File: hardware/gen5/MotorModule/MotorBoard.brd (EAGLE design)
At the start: 60.9 x 49.7 mm, 46 parts, among them IC2 3.3V REG, J1 M20X2SHROUDED

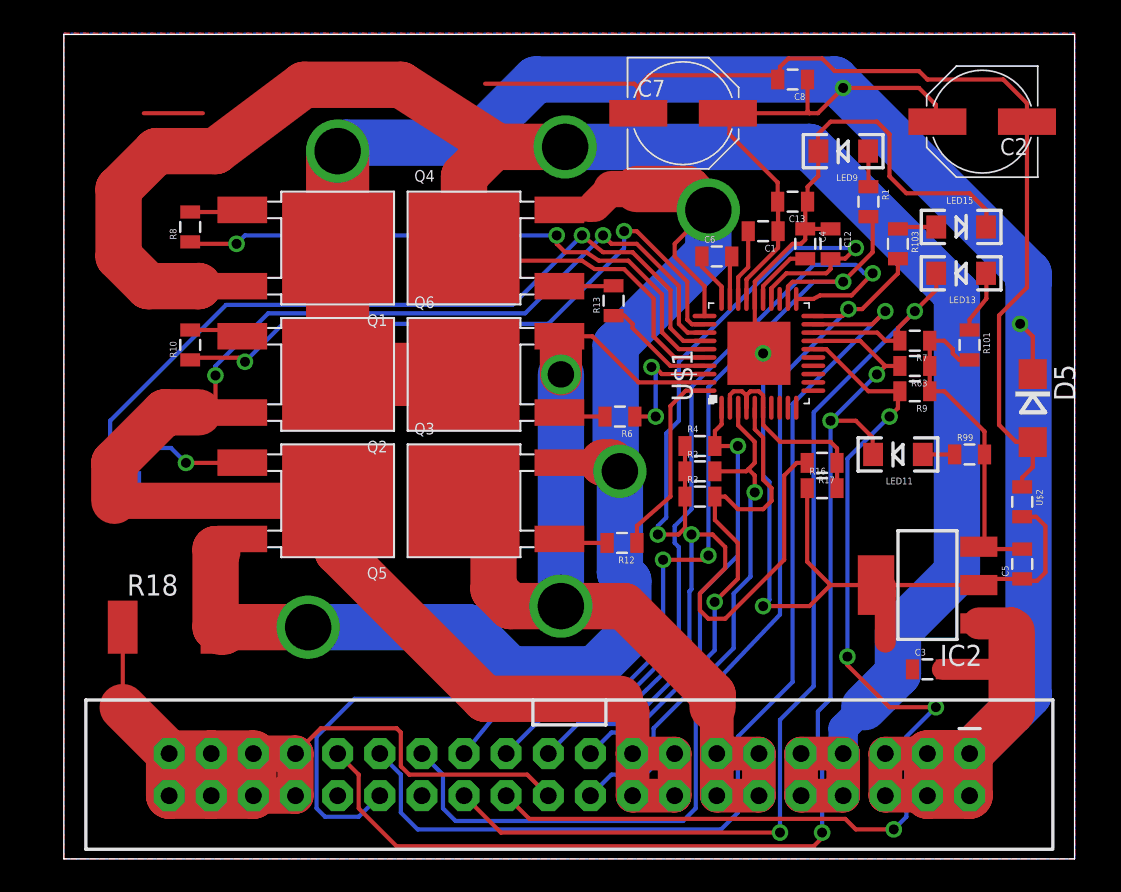
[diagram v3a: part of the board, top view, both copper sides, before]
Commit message: updated motor board
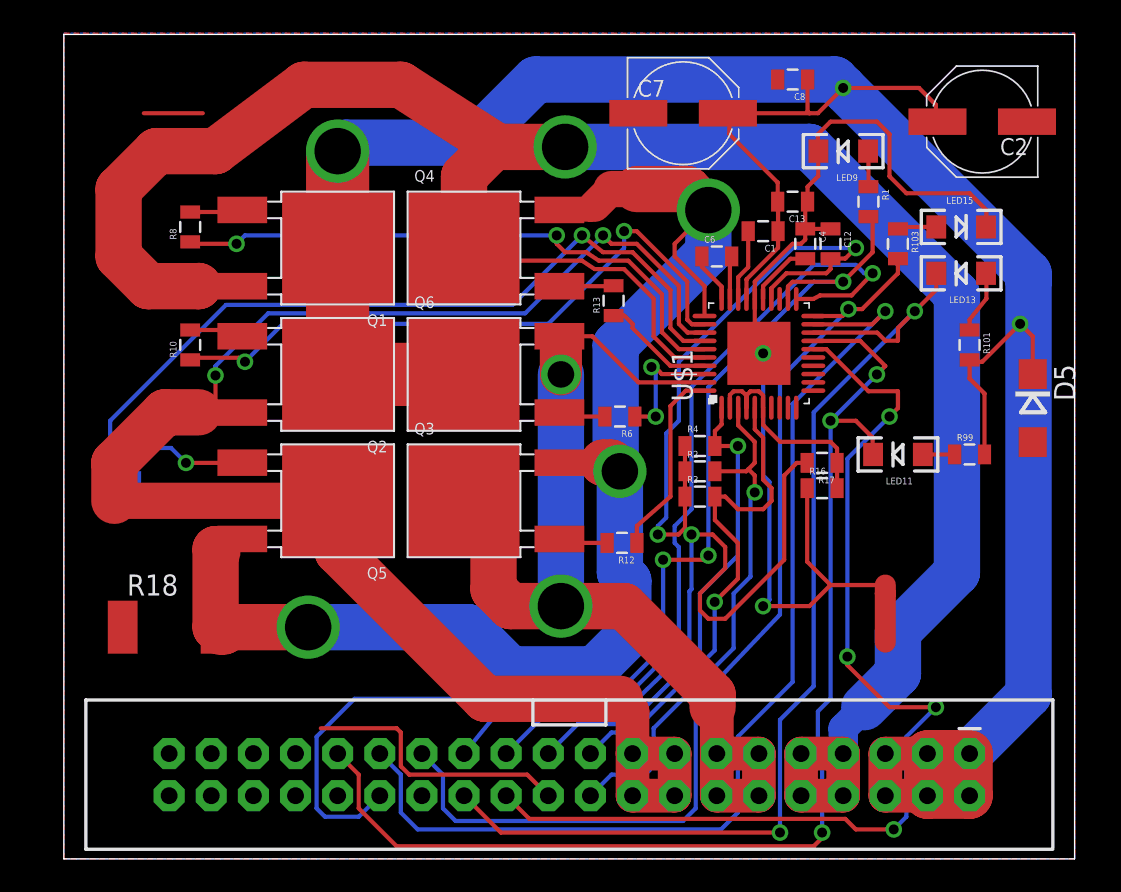
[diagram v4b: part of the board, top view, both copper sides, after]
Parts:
- removed C3, C5: .1uF, SparkFun-Capacitors:0805
- removed IC2: 3.3V REG, linear-technology:SOT223
- removed R63, R7, R9: 1k, SparkFun-Resistors:0805
- removed U$2: INDUCTOR, gen3:0805
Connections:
- removed net 12VGND: C2.-, C3.1, C7.-, C8.2, D5.A, J1.22, J1.33, J1.34, J1.35, J1.36, J1.37, J1.38, J1.39, J1.40, R18.1, U$2.1
- removed net 3.3V: C5.2, IC2.3, R101.2, R63.1, R7.1, R9.1, R99.2
- net 12V: now also R101.2, R99.2; no longer C3.2, IC2.1
- net FAULTN: no longer R63.2
- net GND: now also C2.-, C7.-, C8.2, D5.A, J1.22, J1.33, J1.34, J1.35, J1.36, J1.37, J1.38, J1.39, J1.40, R18.1; no longer C5.1, IC2.2, IC2.4, U$2.2
- net HALLOUT: no longer R9.2
- net LOCKN: no longer R7.2
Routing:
- net 12VGND: track 125.0 -> 0.00 mm
- net 3.3V: track 20.1 -> 0.00 mm
- net GND: track 80.8 -> 86.4 mm
- net 12V: track 171.3 -> 166.4 mm
- net FAULTN: track 73.0 -> 72.1 mm
- added copper zone on layer 1, net GND
- added copper zone on layer 16, net GND
- removed copper zone on layer 1, net 12VGND
- removed copper zone on layer 16, net 12VGND

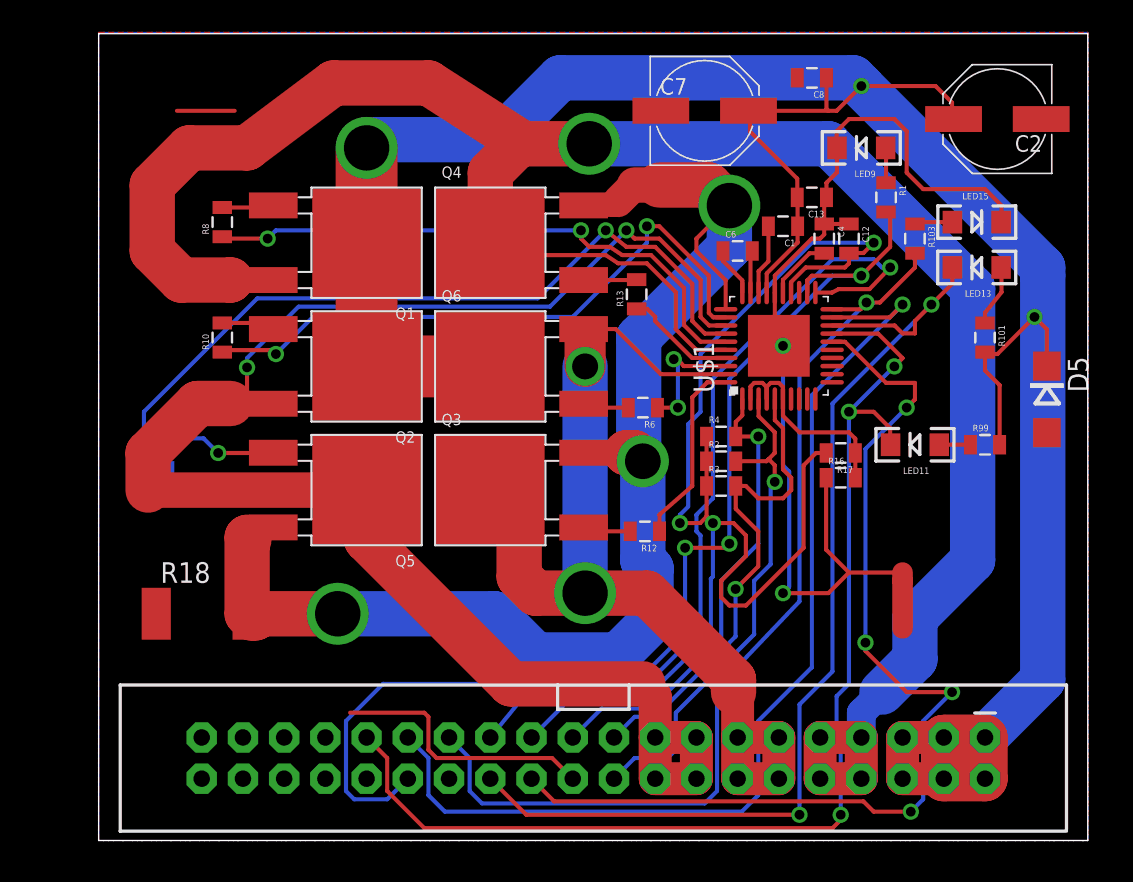
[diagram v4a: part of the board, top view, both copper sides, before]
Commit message: added pullups to the motorboard, and did DRC checking
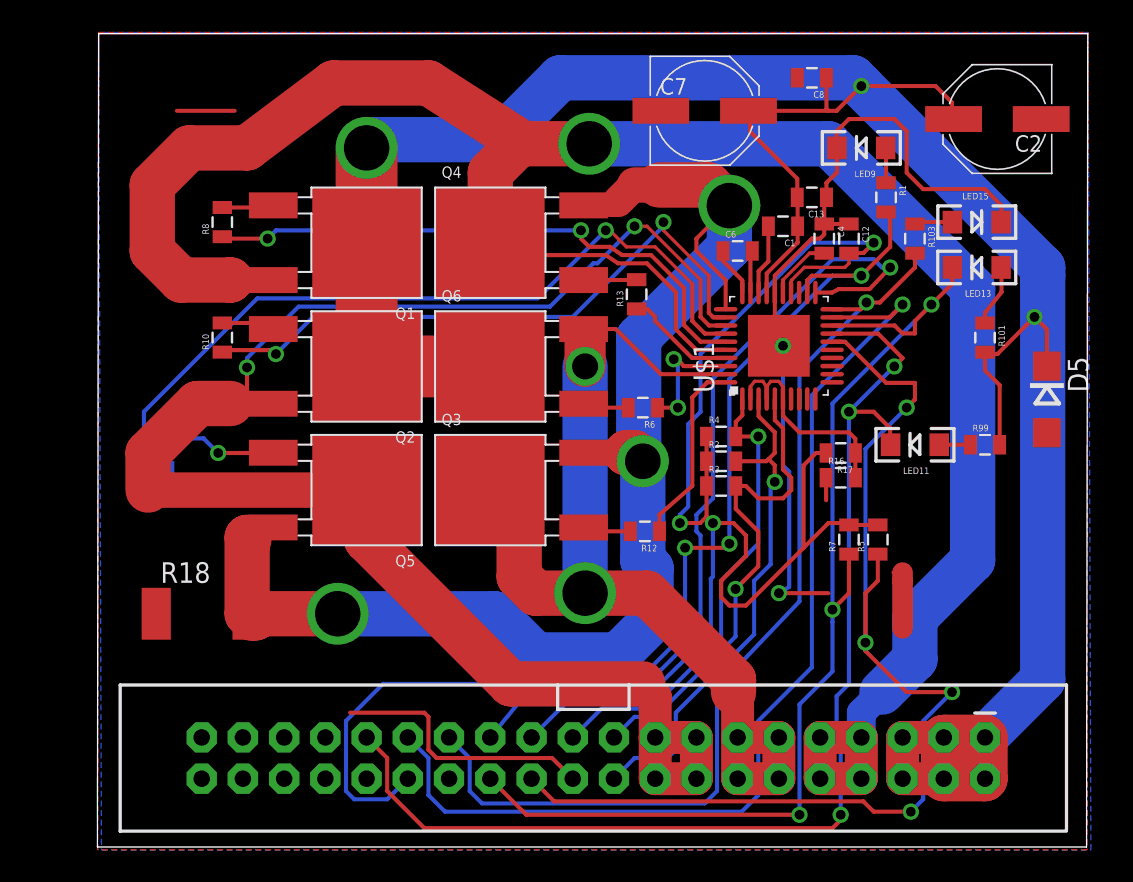
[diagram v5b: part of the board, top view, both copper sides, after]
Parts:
- added R5, R7: 10k, SparkFun-Resistors:0805
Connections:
- net 5V: now also R5.2, R7.2
- net HALLOUT: now also R5.1
- net LOCKN: now also R7.1
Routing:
- net GND: track 86.4 -> 77.3 mm
- net HALLOUT: track 62.9 -> 68.7 mm
- net 5V: track 79.7 -> 85.0 mm
- net LOCKN: track 65.1 -> 68.9 mm, vias 2 -> 3
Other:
- board size 60.9 x 49.7 mm -> 61 x 50.1 mm

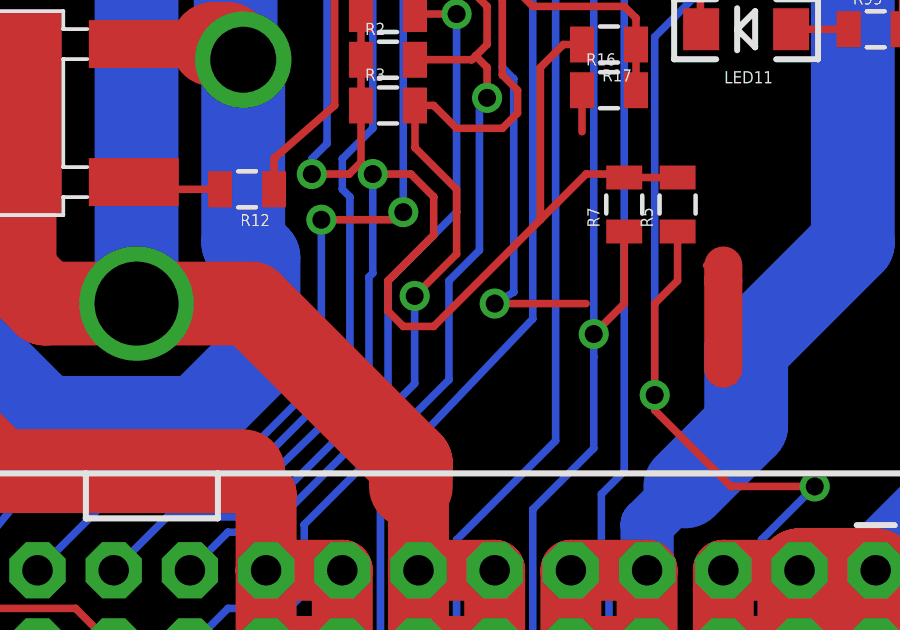
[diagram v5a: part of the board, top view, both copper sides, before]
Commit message: added motorboard gerbers, but noticed some potential issues with grounding afterwards. Checking into it now. It appears that the commsboard is ready to go, however
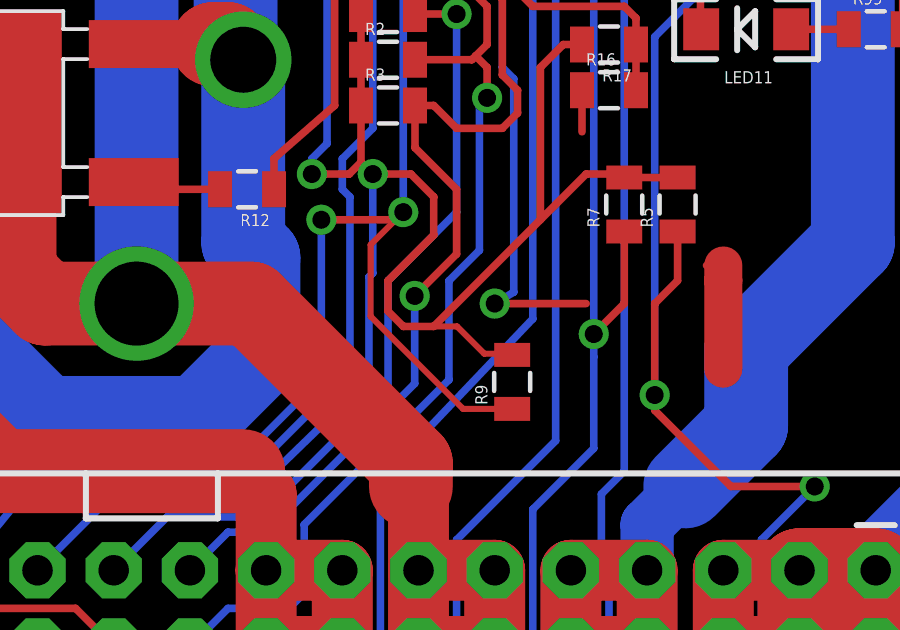
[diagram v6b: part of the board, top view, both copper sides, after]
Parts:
- added R9: 0, SparkFun-Resistors:0805
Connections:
- net 5V: now also R9.2
- net ENABLE: now also R9.1
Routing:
- net ENABLE: track 70.0 -> 79.9 mm
- net 5V: track 85.0 -> 88.1 mm
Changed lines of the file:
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@@
 <wire x1="60.94" y1="49.708" x2="0" y2="49.708" width="0" layer="20"/>
 <wire x1="0" y1="49.708" x2="-0.075796875" y2="-0.398103125" width="0" layer="20"/>
+<dimension x1="60.94" y1="49.708" x2="0" y2="49.708" x3="30.47" y3="53.998428125" textsize="1.778" layer="20" unit="inch"/>
+<dimension x1="61.13459375" y1="-0.5823" x2="60.96" y2="49.784" x3="66.12306875" y3="24.61844375" textsize="1.778" layer="20" unit="inch"/>
 </plain>
 <attributes>
@@
 <element name="R5" library="SparkFun-Resistors" package="0805" value="10k" x="48.006" y="18.542" rot="R90"/>
 <element name="R7" library="SparkFun-Resistors" package="0805" value="10k" x="46.228" y="18.542" rot="R90"/>
+<element name="R9" library="SparkFun-Resistors" package="0805" value="0" x="42.49169375" y="12.629140625" rot="R90"/>
 </elements>
 <signals>
@@
 <wire x1="48.768" y1="36.576" x2="48.768" y2="38.47" width="0.254" layer="1"/>
 <wire x1="48.768" y1="38.47" x2="48.514" y2="38.724" width="0.254" layer="1"/>
+<contactref element="R9" pad="1"/>
+<wire x1="42.49169375" y1="11.729140625" x2="40.85819375" y2="11.729140625" width="0.2032" layer="1"/>
+<wire x1="40.85819375" y1="11.729140625" x2="37.77360625" y2="14.813728125" width="0.2032" layer="1"/>
+<wire x1="37.77360625" y1="14.813728125" x2="37.77360625" y2="17.19960625" width="0.2032" layer="1"/>
+<wire x1="37.77360625" y1="17.19960625" x2="38.862" y2="18.288" width="0.2032" layer="1"/>
 </signal>
 <signal name="DIR">
@@
 <wire x1="42.66030625" y1="34.40530625" x2="42.7151875" y2="34.55069375" width="0.2032" layer="1"/>
 <wire x1="42.7151875" y1="34.55069375" x2="43.480784375" y2="35.316290625" width="0.2032" layer="1"/>
+<contactref element="R9" pad="2"/>
+<wire x1="39.878" y1="14.478" x2="40.654153125" y2="14.478" width="0.2032" layer="1"/>
+<wire x1="40.654153125" y1="14.478" x2="41.562625" y2="13.569528125" width="0.2032" layer="1"/>
+<wire x1="41.562625" y1="13.569528125" x2="42.45130625" y2="13.569528125" width="0.2032" layer="1"/>
+<wire x1="42.45130625" y1="13.569528125" x2="42.49169375" y2="13.529140625" width="0.2032" layer="1"/>
 </signal>
 <signal name="LOCKN">

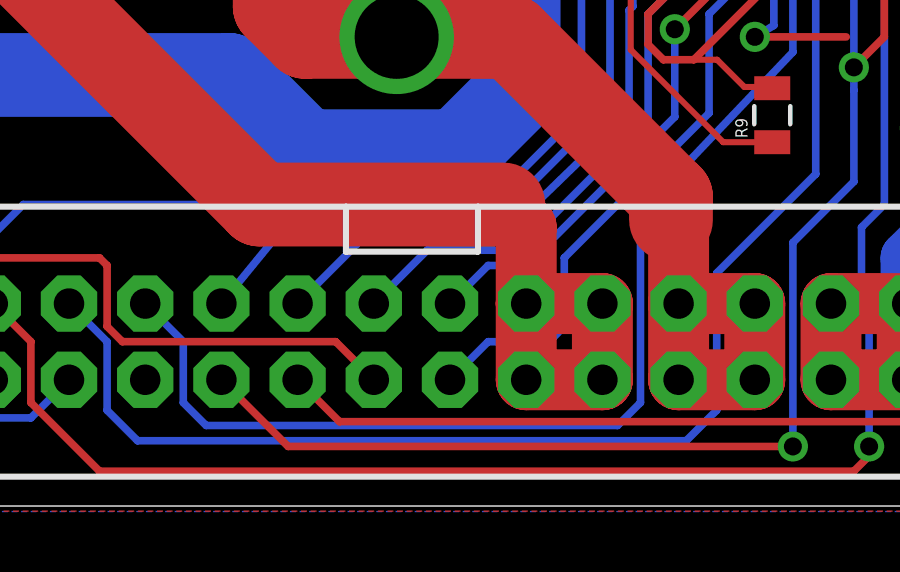
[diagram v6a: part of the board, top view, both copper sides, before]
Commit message: swapped motorboard traces for hallout signals
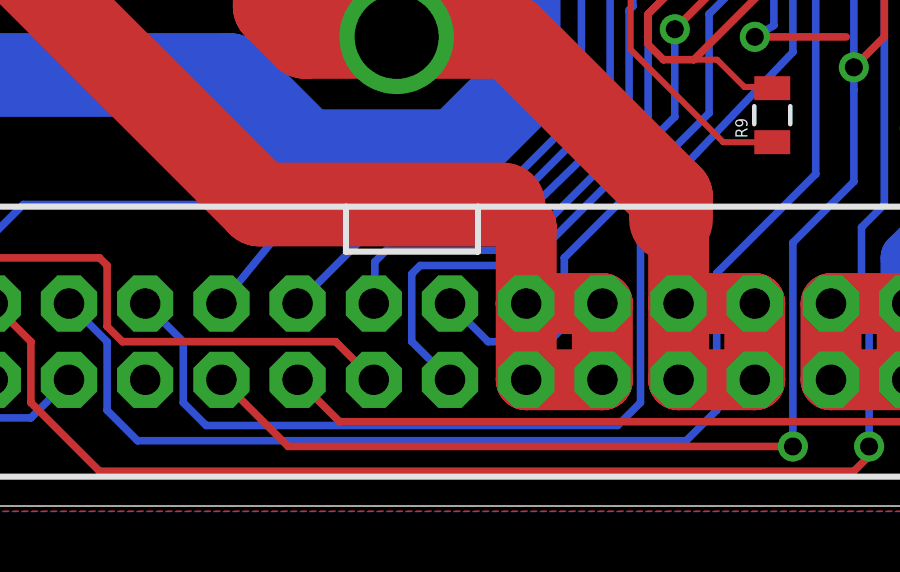
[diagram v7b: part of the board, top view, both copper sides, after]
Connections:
- net M1H1: now also J1.20; no longer J1.19
- net M1H2: now also J1.19; no longer J1.20
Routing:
- net M1H1: track 30.7 -> 35.6 mm
- net M1H3: track 28.9 -> 29.7 mm
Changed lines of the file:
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@@
 <wire x1="38.354" y1="16.002" x2="38.354" y2="12.446" width="0.254" layer="16"/>
 <wire x1="38.354" y1="12.446" x2="34.036" y2="8.128" width="0.254" layer="16"/>
-<wire x1="34.036" y1="8.128" x2="30.988" y2="8.128" width="0.254" layer="16"/>
-<wire x1="30.988" y1="8.128" x2="29.21" y2="6.35" width="0.254" layer="16"/>
+<wire x1="34.036" y1="8.128" x2="29.629253125" y2="8.128" width="0.254" layer="16"/>
+<wire x1="29.629253125" y1="8.128" x2="29.243678125" y2="7.742425" width="0.254" layer="16"/>
+<wire x1="29.243678125" y1="7.742425" x2="29.243678125" y2="6.383678125" width="0.254" layer="16"/>
+<wire x1="29.243678125" y1="6.383678125" x2="29.21" y2="6.35" width="0.254" layer="16"/>
 </signal>
 <signal name="M1H2">
 <contactref element="U$1" pad="3"/>
-<contactref element="J1" pad="20"/>
 <contactref element="R2" pad="2"/>
 <wire x1="40.66" y1="27.201" x2="40.66" y2="26.142" width="0.254" layer="1"/>
@@
 <wire x1="35.56" y1="5.588" x2="35.052" y2="5.08" width="0.254" layer="16"/>
 <wire x1="35.052" y1="5.08" x2="33.02" y2="5.08" width="0.254" layer="16"/>
-<wire x1="33.02" y1="5.08" x2="31.75" y2="3.81" width="0.254" layer="16"/>
 <wire x1="40.386" y1="12.7" x2="35.56" y2="7.874" width="0.254" layer="16"/>
 <wire x1="35.56" y1="7.874" x2="35.56" y2="5.588" width="0.254" layer="16"/>
+<contactref element="J1" pad="19"/>
+<wire x1="33.02" y1="5.08" x2="31.75" y2="6.35" width="0.254" layer="16"/>
 </signal>
 <signal name="M1H1">
 <contactref element="U$1" pad="5"/>
-<contactref element="J1" pad="19"/>
 <contactref element="R3" pad="2"/>
 <wire x1="41.66" y1="27.201" x2="41.66" y2="25.904" width="0.254" layer="1"/>
@@
 <wire x1="39.116" y1="21.706" x2="39.254" y2="21.844" width="0.254" layer="1"/>
 <wire x1="39.243" y1="12.573" x2="34.29" y2="7.62" width="0.254" layer="16"/>
-<wire x1="34.29" y1="7.62" x2="33.02" y2="7.62" width="0.254" layer="16"/>
-<wire x1="33.02" y1="7.62" x2="31.75" y2="6.35" width="0.254" layer="16"/>
 <wire x1="39.243" y1="15.494" x2="40.64" y2="16.891" width="0.254" layer="1"/>
 <wire x1="40.64" y1="16.891" x2="40.64" y2="19.05" width="0.254" layer="1"/>
 <wire x1="40.64" y1="19.05" x2="39.254" y2="20.436" width="0.254" layer="1"/>
 <wire x1="39.254" y1="20.436" x2="39.254" y2="21.844" width="0.254" layer="1"/>
+<contactref element="J1" pad="20"/>
+<wire x1="34.29" y1="7.62" x2="30.75511875" y2="7.62" width="0.254" layer="16"/>
+<wire x1="30.75511875" y1="7.62" x2="30.475515625" y2="7.340396875" width="0.254" layer="16"/>
+<wire x1="30.475515625" y1="7.340396875" x2="30.475515625" y2="5.084484375" width="0.254" layer="16"/>
+<wire x1="30.475515625" y1="5.084484375" x2="31.75" y2="3.81" width="0.254" layer="16"/>
 </signal>
 <signal name="PWM">
